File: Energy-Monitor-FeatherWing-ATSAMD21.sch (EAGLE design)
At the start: 32 parts

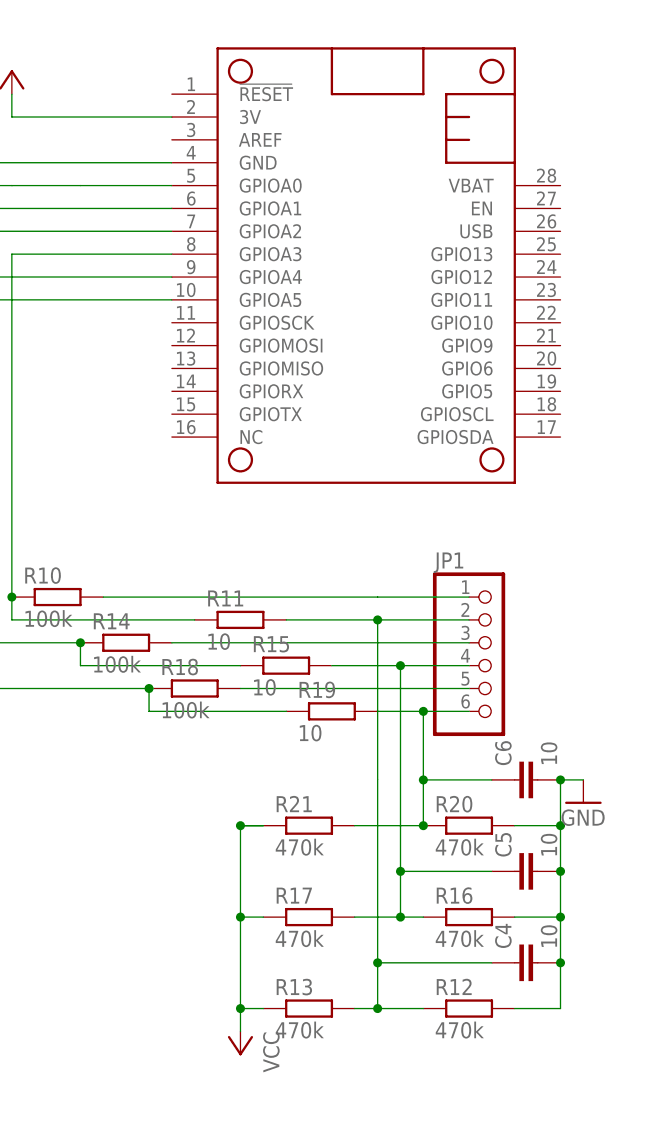
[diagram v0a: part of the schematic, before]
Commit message: Fix layout issues - the TRS jacks have a rim that is not flush with the PCB, had to sacrifice some FeatherWing pins.
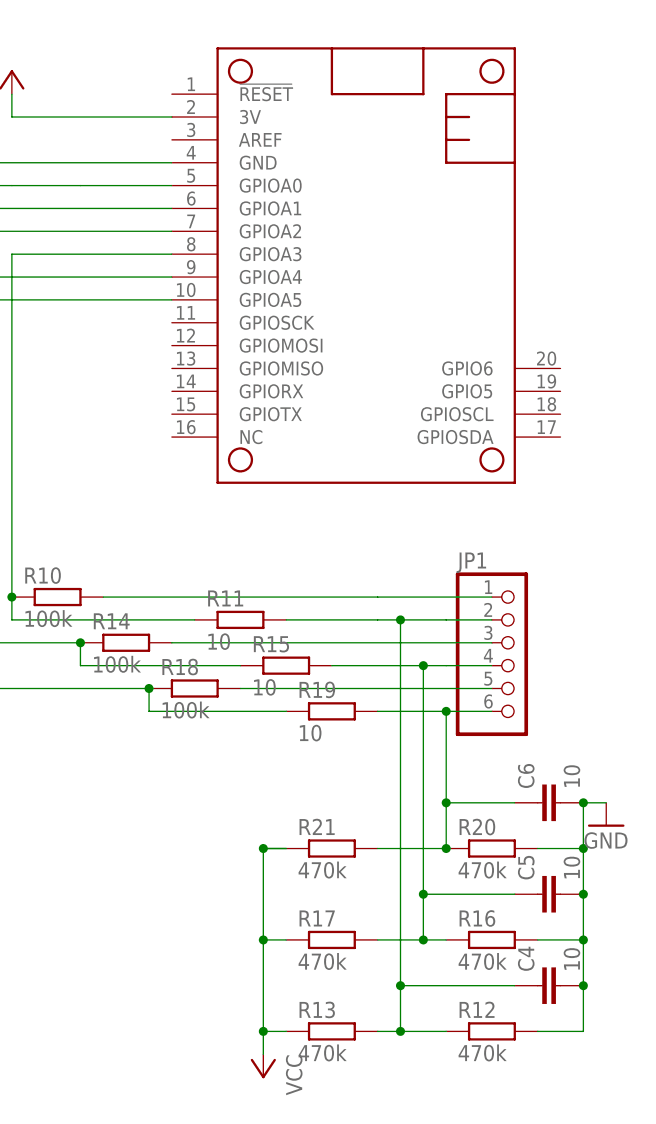
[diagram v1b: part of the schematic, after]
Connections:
- net N$6 renamed AC_GND
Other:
- moved on the sheet: C4, C5, C6, JP1, R12, R13, R16, R17, R20, R21

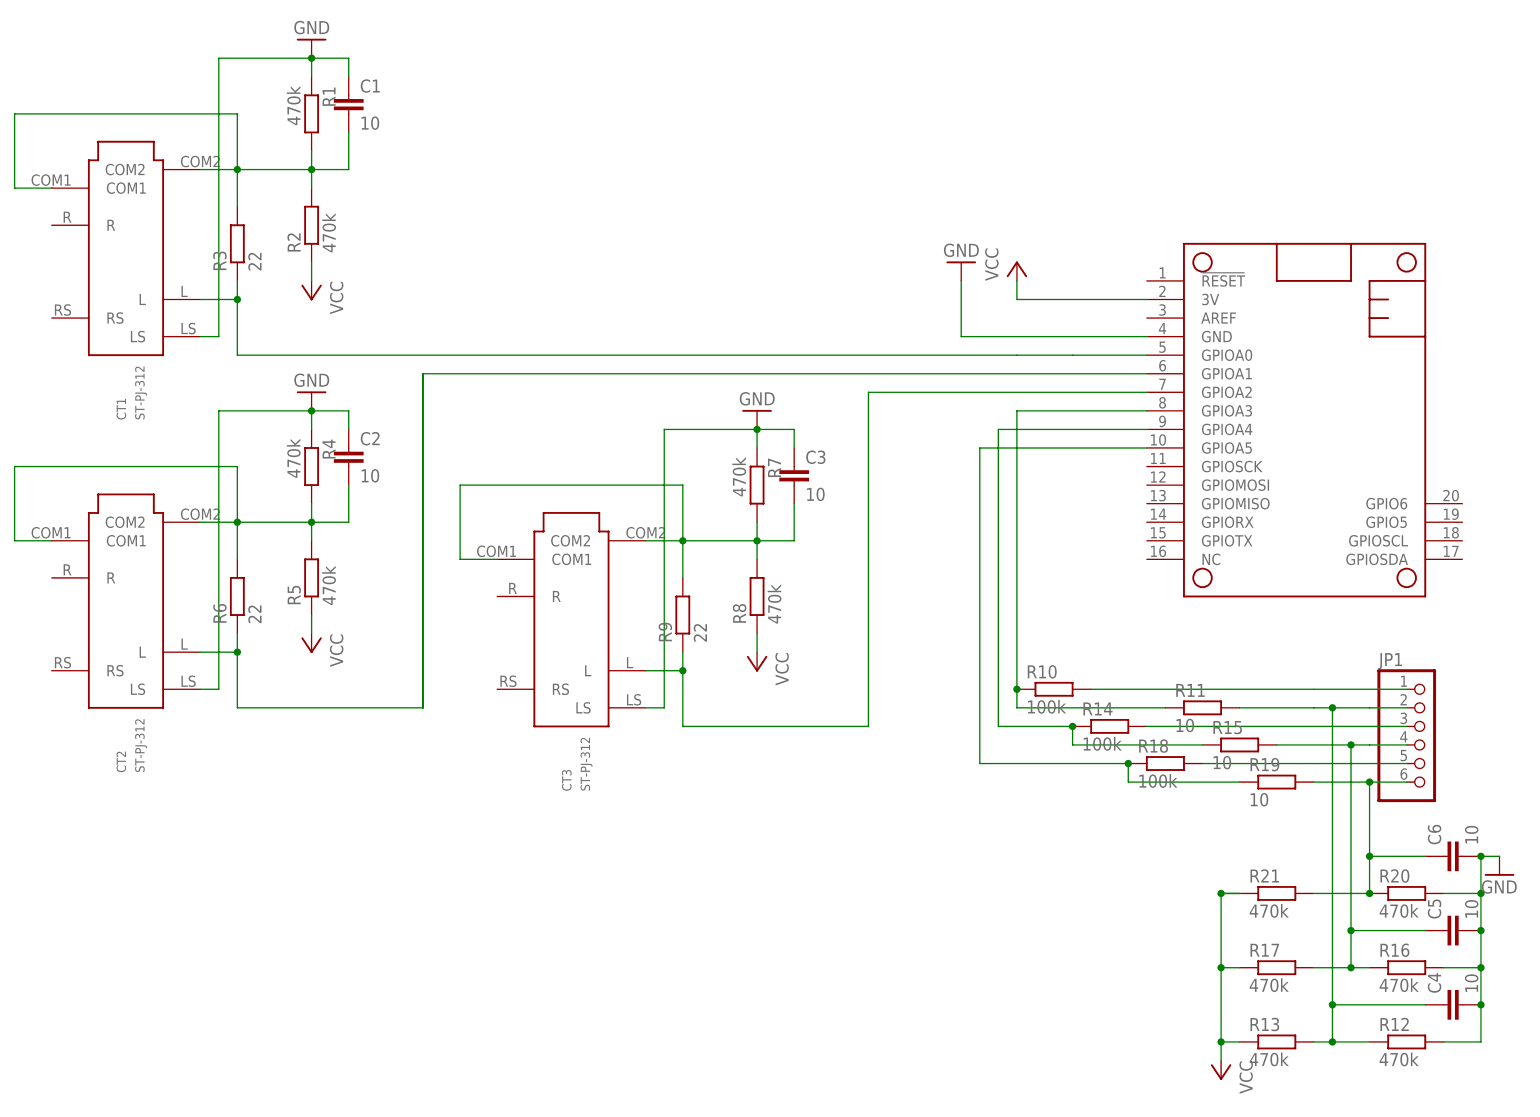
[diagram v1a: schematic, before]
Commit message: Layout cleanup; add hints for PCBA
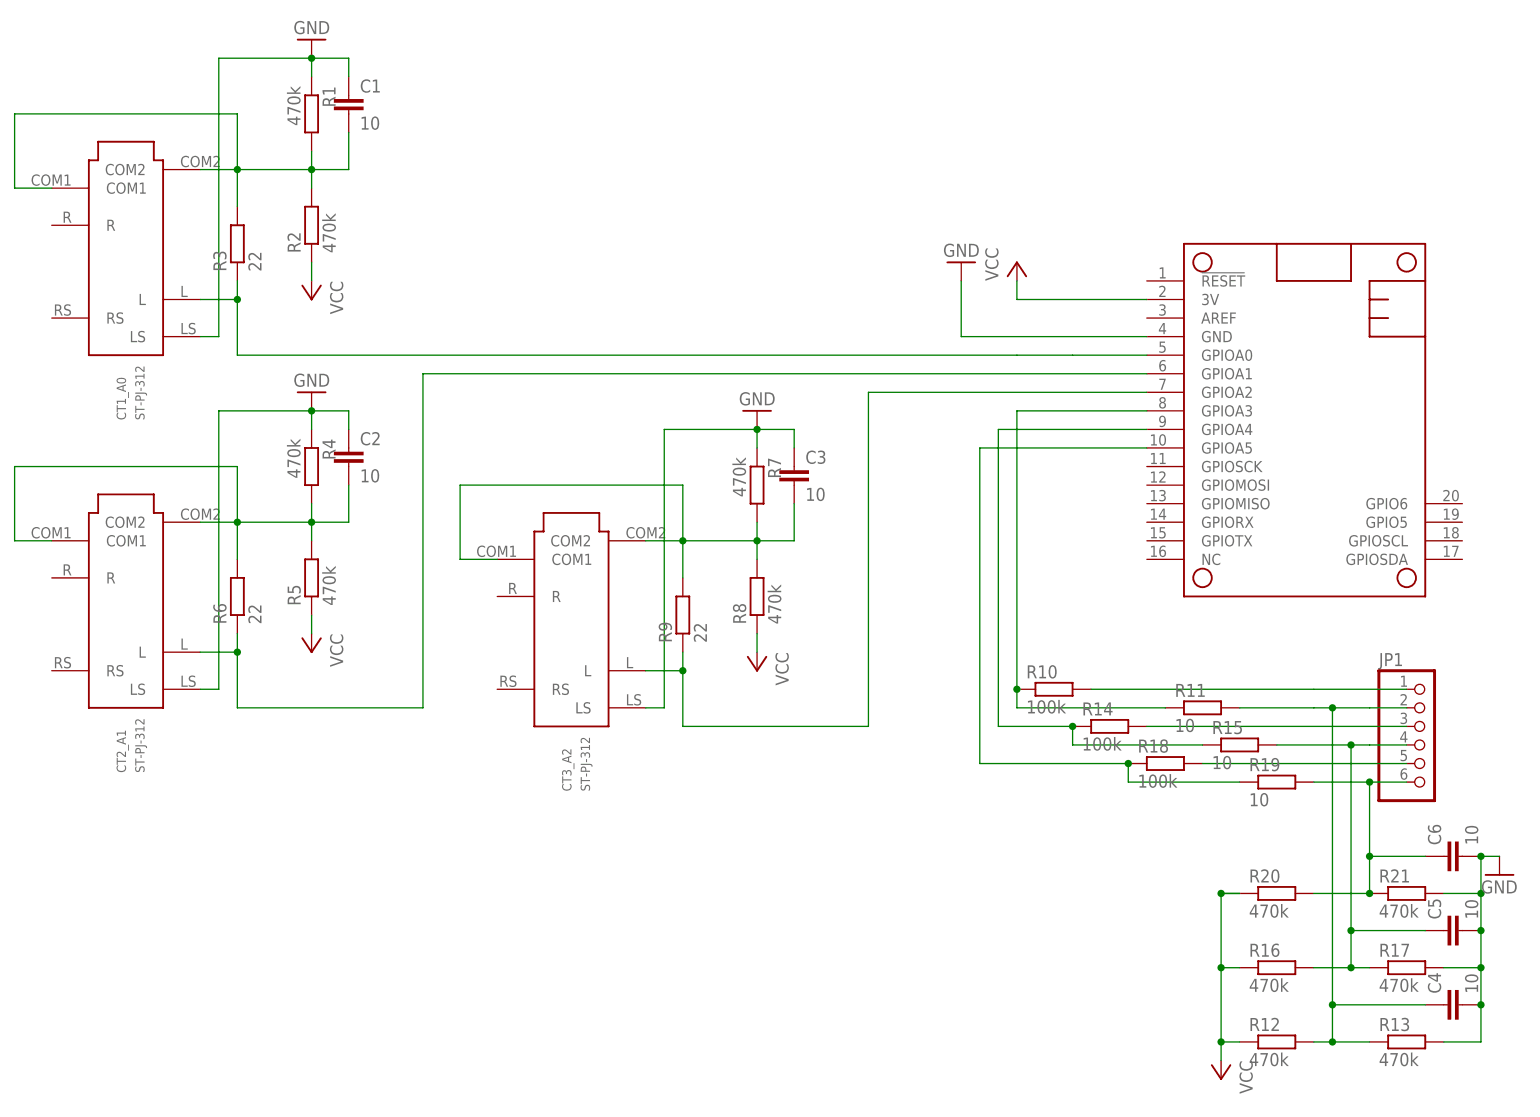
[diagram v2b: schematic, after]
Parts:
- renumbered CT1 to CT1_A0, CT2 to CT2_A1, CT3 to CT3_A2
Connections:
- net AC_GND: now also R20.2, R21.1; no longer R20.1, R21.2
- net GND: now also R13.2, R17.2, R21.2; no longer R12.2, R16.2, R20.2
- net N$6: now also R16.2, R17.1; no longer R16.1, R17.2
- net N$9: now also R12.2, R13.1; no longer R12.1, R13.2
- net VCC: now also R12.1, R16.1, R20.1; no longer R13.1, R17.1, R21.1
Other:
- moved on the sheet: R12, R13, R16, R17, R20, R21
